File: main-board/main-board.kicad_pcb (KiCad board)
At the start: 2 copper layers, 74 parts, among them J1 NVIDIA_Jetson_NX_Dev_40pin_Co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, J10 FSESC_6.6_COMM, J11 FSESC_6.6_COMM, J12 FSESC_6.6_COMM, J13 FSESC_6.6_COMM, J14 FSESC_6.6_COMM, J2 NVIDIA_Jetson_NX_Dev_Button_C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, J3 Conn_01x02, J4 Conn_01x02, J5 Conn_01x02, J6 Conn_01x02, J7 QWIIC_Generic_Conn, J8 Conn_01x03, J9 FSESC_6.6_COMM, M1 Fan_3pin, M2 Fan_3pin, M3 Fan_3pin, Q1 Q_NMOS_GSD, Q2 Q_NMOS_GSD, Q3 Q_NMOS_GSD, Q4 Q_NMOS_GSD, Q5 Q_NMOS_GSD, Q6 Q_NMOS_GSD, Q7 Q_NMOS_GSD, Q8 Q_NMOS_GSD, U1 RFM95W_Adafruit_Breakout, U10 Analog Temp Sensor, U11 Adafruit_GPS_V3, U12 SN74AHCT125D, U2 TDK_I3A4W008A033V, U3 TDK_I3A4W008A033V, U4 PYBE30-Q24-S24, U5 Teensy_4.1, U6 Analog Temp Sensor, U7 Analog Temp Sensor, U8 Analog Temp Sensor, U9 Analog Temp Sensor

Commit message: ahhh i messed some stuff up
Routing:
- net /NX_SDA: track 55.0 -> 0.00 mm
- net /NX_SCL: track 52.3 -> 0.00 mm
- net GND: track 32.5 -> 0.09 mm
- net +5V: track 19.4 -> 0.00 mm
- net +BATT: track 16.6 -> 0.00 mm
- net +12V: track 14.7 -> 0.00 mm
- net /ADC_BATT: track 10.9 -> 0.00 mm
- net /ADC_5V: track 11.1 -> 0.76 mm
- net /ADC_12V: track 10.9 -> 0.74 mm
- net /ADC_24V: track 10.9 -> 0.74 mm
- net Net-(J8-Pad3): track 9.97 -> 0.00 mm
- net +24V: track 9.14 -> 0.00 mm
- net Net-(D12-Pad2): track 8.64 -> 0.00 mm
- net Net-(D11-Pad2): track 8.64 -> 0.00 mm
- net Net-(R5-Pad2): track 8.10 -> 0.00 mm
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
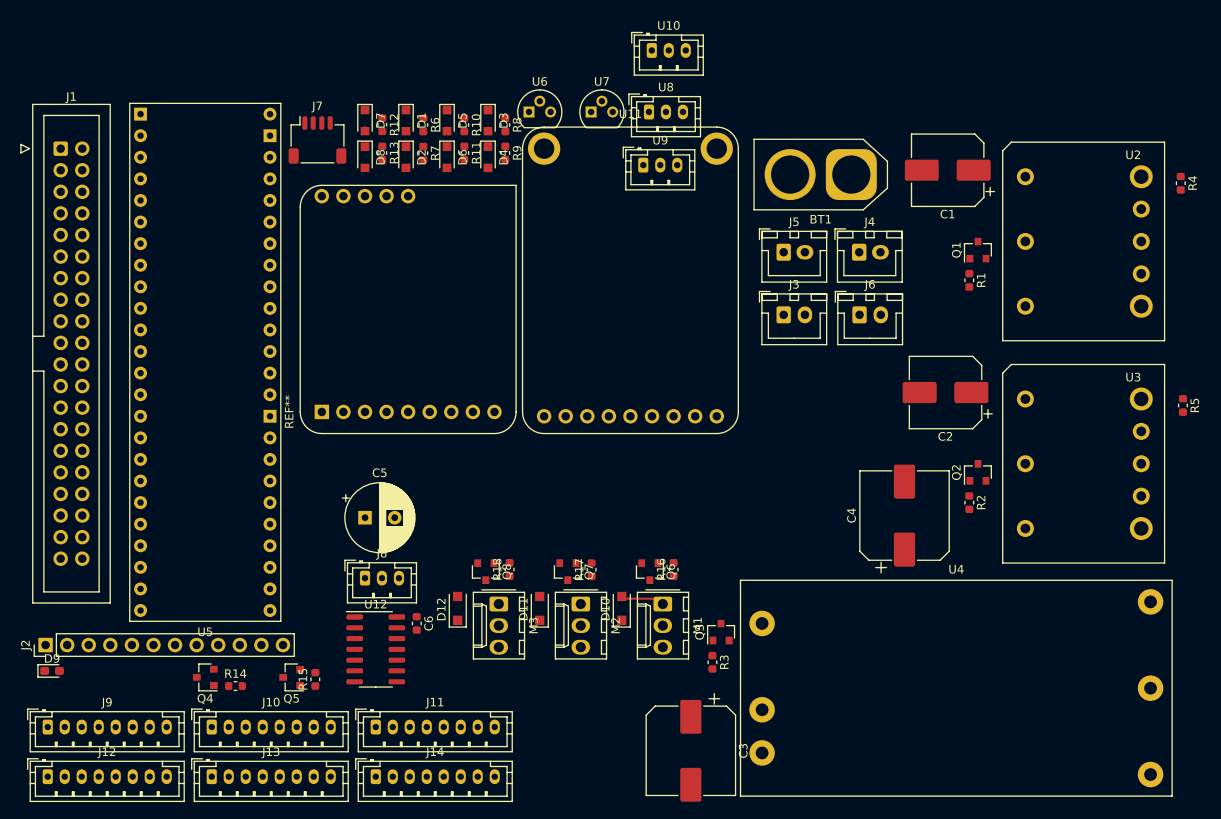
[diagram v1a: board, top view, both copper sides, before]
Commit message: Removed 24V connector, Changed net switch power bus, changed motor driver connector
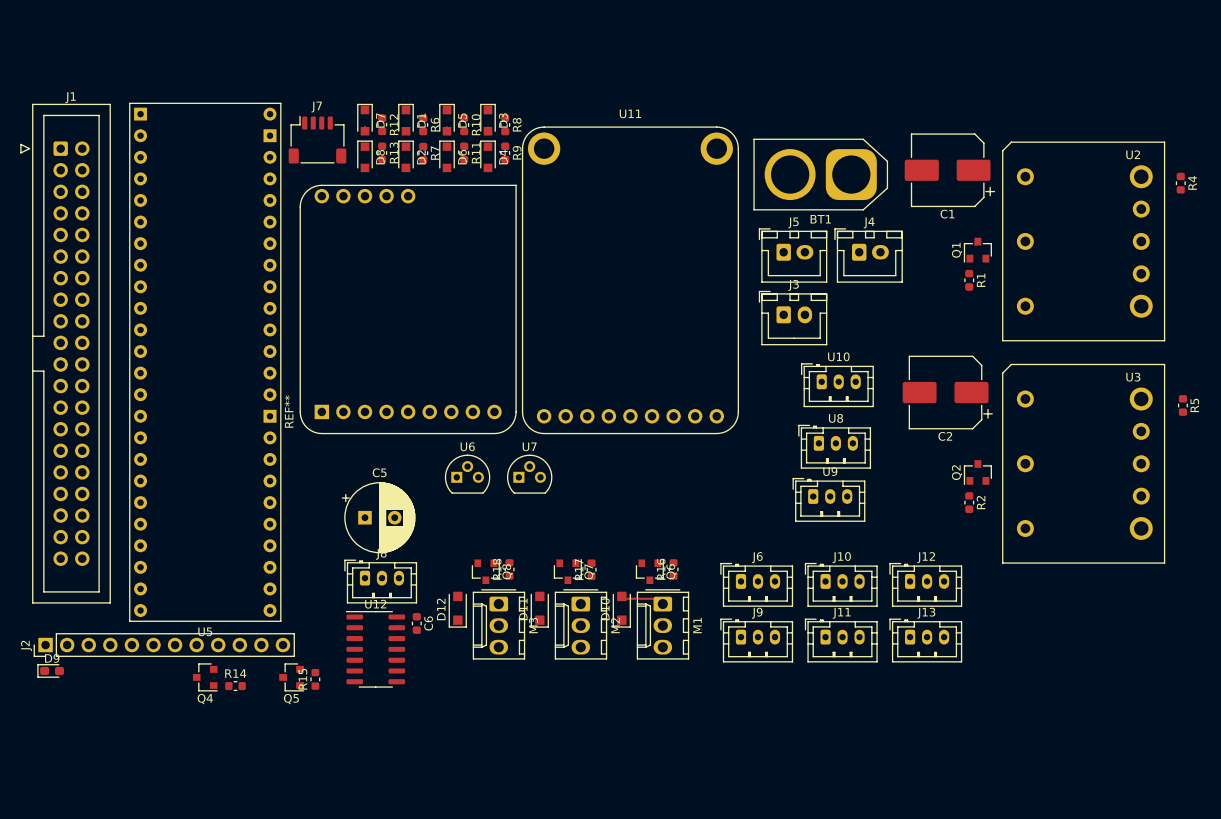
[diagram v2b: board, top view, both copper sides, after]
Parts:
- removed C3, C4: 100u, Capacitor_SMD:CP_Elec_10x10
- removed J14: FSESC_6.6_COMM, Connector_JST:JST_PH_B8B-PH-K_1x08_P2.00mm_Vertical
- removed Q3: Q_NMOS_GSD, Package_TO_SOT_SMD:SOT-23
- removed R3: 100k, Resistor_SMD:R_0603_1608Metric
- removed U4: PYBE30-Q24-S24, ASTRA_Footprints:PYBE30
- J10, J11, J12, J13, J9: value FSESC_6.6_COMM -> FSESC_6.6_COMM_Minimal; footprint Connector_JST:JST_PH_B8B-PH-K_1x08_P2.00mm_Vertical -> Connector_JST:JST_PH_B3B-PH-K_1x03_P2.00mm_Vertical
- J6: value Conn_01x02 -> FSESC_6.6_COMM_Minimal; footprint Connector_JST:JST_XH_B2B-XH-A_1x02_P2.50mm_Vertical -> Connector_JST:JST_PH_B3B-PH-K_1x03_P2.00mm_Vertical
- moved J12 104.1 mm to (127.4, 102.5)
- moved J13 83.8 mm to (127.4, 109.0)
- moved J9 82.3 mm to (107.5, 109.0)
- moved J10 74.2 mm to (117.5, 102.5)
- moved J11 54.0 mm to (117.5, 109.0)
- moved U6 43.8 mm to (74.0, 90.2)
- moved U7 43.8 mm to (81.4, 90.2)
- moved U10 43.8 mm to (117.0, 79.0)
- moved U8 43.8 mm to (116.7, 86.2)
- moved U9 43.8 mm to (116.0, 92.5)
- moved J6 34.3 mm to (107.5, 102.5)
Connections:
- J10 pad 1: Net-(J10-Pad1) -> GND
- J10 pad 2: Net-(J10-Pad2) -> /M3_RX
- J10 pad 3: GND -> /M3_TX
- J11 pad 1: Net-(J11-Pad1) -> GND
- J11 pad 2: Net-(J11-Pad2) -> /M4_RX
- J11 pad 3: GND -> /M4_TX
- J12 pad 1: Net-(J12-Pad1) -> GND
- J12 pad 2: Net-(J12-Pad2) -> /M5_RX
- J12 pad 3: GND -> /M5_TX
- J13 pad 1: Net-(J13-Pad1) -> GND
- J13 pad 2: Net-(J13-Pad2) -> /M6_RX
- J13 pad 3: GND -> /M6_TX
- J4 pad 1: +12V -> +5V
- J6 pad 1: +24V -> GND
- J6 pad 2: GND -> /M1_RX
- J9 pad 1: Net-(J9-Pad1) -> GND
- J9 pad 2: Net-(J9-Pad2) -> /M2_RX
- J9 pad 3: GND -> /M2_TX
- U5 pad 24: /24V_Disable -> Net-(U5-Pad24)
- U5 pad 44: /ADC_24V -> Net-(U5-Pad44)

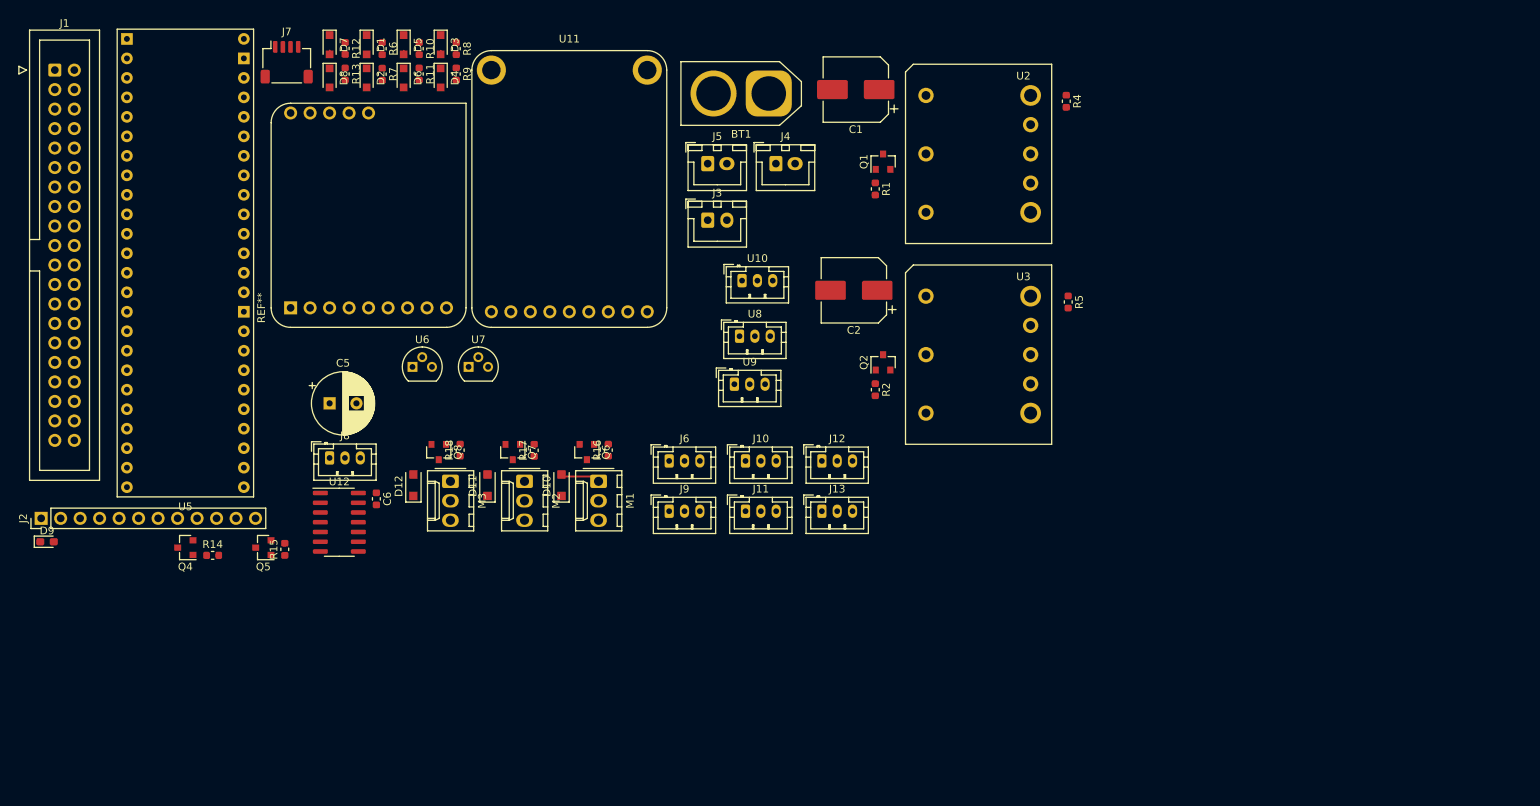
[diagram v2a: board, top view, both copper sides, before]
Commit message: Worked on PCB layout
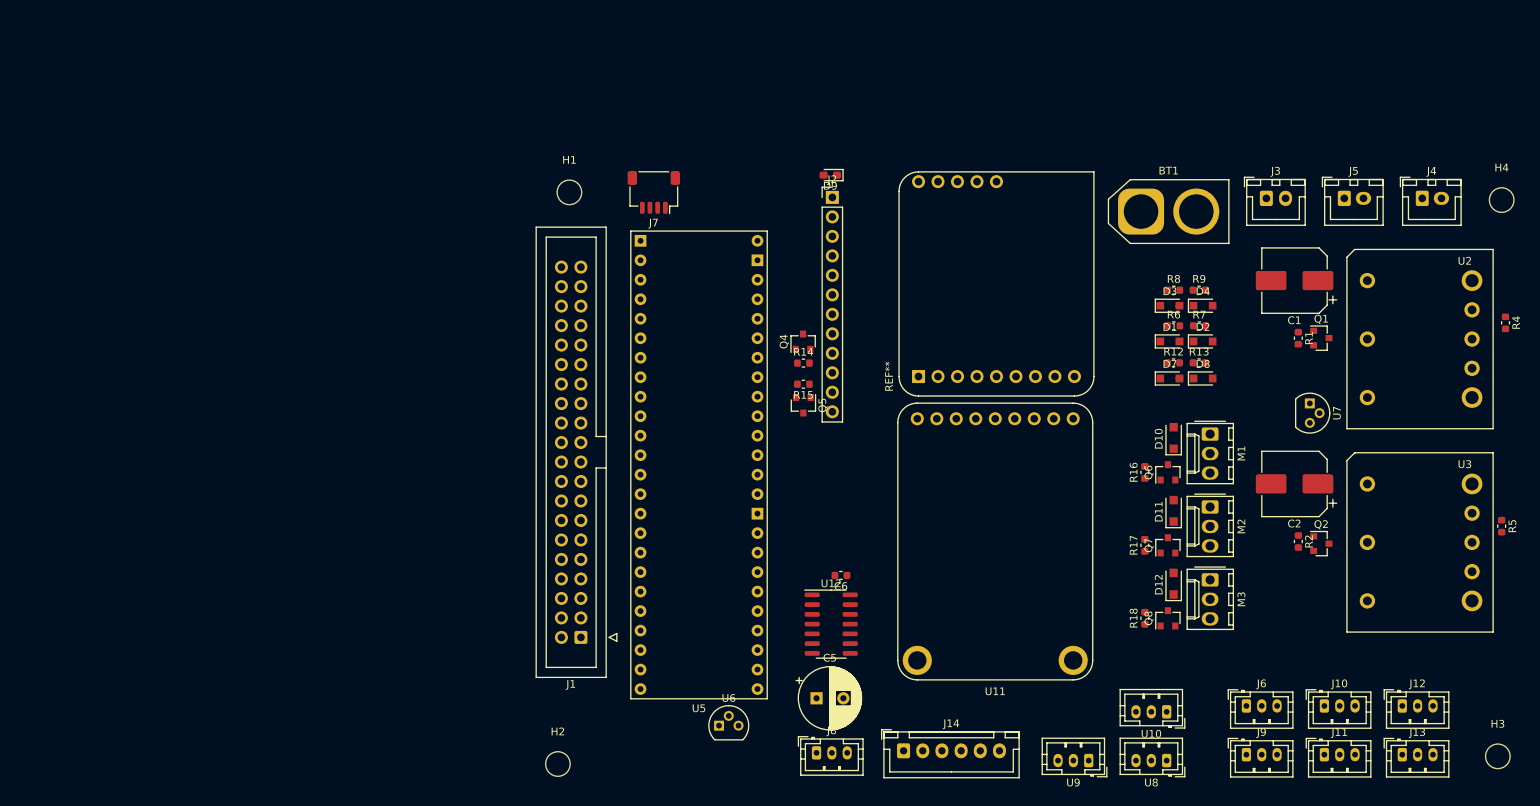
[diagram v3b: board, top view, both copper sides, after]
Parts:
- removed D5, D6: D_Schottky_Small, Diode_SMD:D_SOD-323_HandSoldering
- removed R10: 80.6k, Resistor_SMD:R_0603_1608Metric
- removed R11: 10k, Resistor_SMD:R_0603_1608Metric
- added H1: MountingHole, MountingHole:MountingHole_3.2mm_M3, F.Cu at (94.5, 67.5)
- added H2: MountingHole, MountingHole:MountingHole_3.2mm_M3, F.Cu at (93.0, 142.0)
- added H3: MountingHole, MountingHole:MountingHole_3.2mm_M3, F.Cu at (215.5, 141.0)
- added H4: MountingHole, MountingHole:MountingHole_3.2mm_M3, F.Cu at (216.0, 68.5)
- added J14: ArducamPTZ, Connector_JST:JST_XH_B6B-XH-A_1x06_P2.50mm_Vertical, F.Cu at (138.1, 140.3)
- moved D8 120.4 mm to (177.1, 91.8), turned to 0 degrees
- moved D7 117.8 mm to (172.8, 91.8), turned to 0 degrees
- moved R13 117.5 mm to (176.6, 89.7), turned to 0 degrees
- moved R12 115.5 mm to (173.2, 89.7), turned to 0 degrees
- moved D2 114.3 mm to (177.1, 86.9), turned to 0 degrees
- moved D9 112.7 mm to (128.5, 65.2), turned to 180 degrees
- moved D1 111.6 mm to (172.8, 86.9), turned to 0 degrees
- moved R7 111.4 mm to (176.6, 84.9), turned to 0 degrees
- moved J2 111.3 mm to (128.8, 68.2), turned to 0 degrees
- moved U7 109.7 mm to (191.0, 95.0), turned to 270 degrees
- moved R6 109.3 mm to (173.3, 84.9), turned to 0 degrees
- moved D4 103.7 mm to (177.1, 82.3), turned to 0 degrees
- moved D3 100.9 mm to (172.8, 82.3), turned to 0 degrees
- moved J1 100.8 mm to (96.0, 125.5), turned to 180 degrees
- moved R9 100.8 mm to (176.6, 80.2), turned to 0 degrees
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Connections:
- J1 pad 1: Net-(J1-Pad1) -> (no net)
- J1 pad 10: Net-(J1-Pad10) -> (no net)
- J1 pad 11: Net-(J1-Pad11) -> (no net)
- J1 pad 12: Net-(J1-Pad12) -> (no net)
- J1 pad 13: Net-(J1-Pad13) -> (no net)
- J1 pad 15: Net-(J1-Pad15) -> (no net)
- J1 pad 16: Net-(J1-Pad16) -> (no net)
- J1 pad 17: Net-(J1-Pad17) -> (no net)
- J1 pad 18: Net-(J1-Pad18) -> (no net)
- J1 pad 19: Net-(J1-Pad19) -> (no net)
- J1 pad 2: Net-(J1-Pad2) -> (no net)
- J1 pad 21: Net-(J1-Pad21) -> (no net)
- J1 pad 22: Net-(J1-Pad22) -> (no net)
- J1 pad 23: Net-(J1-Pad23) -> (no net)
- J1 pad 24: Net-(J1-Pad24) -> (no net)
- J1 pad 26: Net-(J1-Pad26) -> (no net)
- J1 pad 27: Net-(J1-Pad27) -> (no net)
- J1 pad 28: Net-(J1-Pad28) -> (no net)
- J1 pad 29: Net-(J1-Pad29) -> (no net)
- J1 pad 31: Net-(J1-Pad31) -> (no net)
- J1 pad 32: Net-(J1-Pad32) -> (no net)
- J1 pad 33: Net-(J1-Pad33) -> (no net)
- J1 pad 35: Net-(J1-Pad35) -> (no net)
- J1 pad 36: Net-(J1-Pad36) -> (no net)
- J1 pad 37: Net-(J1-Pad37) -> (no net)
- J1 pad 38: Net-(J1-Pad38) -> (no net)
- J1 pad 4: Net-(J1-Pad4) -> (no net)
- J1 pad 40: Net-(J1-Pad40) -> (no net)
- J1 pad 7: Net-(J1-Pad7) -> (no net)
- J1 pad 8: Net-(J1-Pad8) -> (no net)
- J2 pad 10: Net-(J2-Pad10) -> (no net)
- J2 pad 3: Net-(J2-Pad3) -> (no net)
- J2 pad 4: Net-(J2-Pad4) -> (no net)
- J2 pad 5: Net-(J2-Pad5) -> (no net)
- J2 pad 6: Net-(J2-Pad6) -> (no net)
- M1 pad 3: Net-(M1-Pad3) -> (no net)
- M2 pad 3: Net-(M2-Pad3) -> (no net)
- M3 pad 3: Net-(M3-Pad3) -> (no net)
- U1 pad 11: Net-(U1-Pad11) -> (no net)
- U1 pad 12: Net-(U1-Pad12) -> (no net)
- U1 pad 13: Net-(U1-Pad13) -> (no net)
- U1 pad 14: Net-(U1-Pad14) -> (no net)
- U1 pad 15: Net-(U1-Pad15) -> (no net)
- U1 pad 3: Net-(U1-Pad3) -> (no net)
- U11 pad 1: Net-(U11-Pad1) -> (no net)
- U11 pad 2: Net-(U11-Pad2) -> (no net)
- U11 pad 3: Net-(U11-Pad3) -> (no net)
- U11 pad 4: Net-(U11-Pad4) -> (no net)
- U11 pad 9: Net-(U11-Pad9) -> (no net)
- U2 pad 5: Net-(U2-Pad5) -> (no net)
- U3 pad 5: Net-(U3-Pad5) -> (no net)
- U5 pad 11: Net-(U5-Pad11) -> (no net)
- U5 pad 15: Net-(U5-Pad15) -> (no net)
- U5 pad 24: Net-(U5-Pad24) -> (no net)
- U5 pad 38: Net-(U5-Pad38) -> (no net)
- U5 pad 39: Net-(U5-Pad39) -> (no net)
- U5 pad 44: Net-(U5-Pad44) -> (no net)
- U5 pad 45: Net-(U5-Pad45) -> (no net)
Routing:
- net Net-(D10-Pad2): track 5.09 -> 0.00 mm
- net /ADC_24V: track 0.74 -> 0.00 mm

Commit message: Started routing
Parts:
- moved J7 65.3 mm to (99.0, 132.5), turned to 270 degrees
- moved D4 59.1 mm to (123.1, 106.3)
- moved R8 59.1 mm to (119.3, 104.2)
- moved R9 59.1 mm to (122.6, 104.2)
- moved D3 59.1 mm to (118.8, 106.3)
- moved D8 57.2 mm to (123.1, 110.8)
- moved R12 57.2 mm to (119.2, 108.7)
- moved R13 57.2 mm to (122.6, 108.7)
- moved D7 57.2 mm to (118.8, 110.8)
- moved D2 56.0 mm to (123.1, 101.9)
- moved R6 56.0 mm to (119.3, 99.9)
- moved D1 56.0 mm to (118.8, 101.9)
- moved R7 56.0 mm to (122.6, 99.9)
- moved Q5 49.0 mm to (105.5, 140.2)
- moved R14 49.0 mm to (105.5, 134.8)
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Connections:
- U5 pad 16: /GPS_TX -> GND
- U5 pad 17: /GPS_RX -> /M3_TX
- U5 pad 18: /ADC3 -> /SCK
- U5 pad 19: /ADC4 -> /M3_RX
- U5 pad 20: /M5_RX -> (no net)
- U5 pad 21: /M5_TX -> (no net)
- U5 pad 22: /12V_Disable -> /ADC1
- U5 pad 23: /5V_Disable -> /ADC2
- U5 pad 24: (no net) -> /M4_TX
- U5 pad 25: /Fan1_Control -> /M4_RX
- U5 pad 26: /M6_RX -> (no net)
- U5 pad 27: /M6_TX -> (no net)
- U5 pad 28: /Fan2_Control -> +3V3
- U5 pad 29: /Fan3_Control -> GND
- U5 pad 30: /ADC_5V -> +5V
- U5 pad 31: /ADC_12V -> /GPS_TX
- U5 pad 32: /ADC_BATT -> /GPS_RX
- U5 pad 33: /ADC5 -> /ADC3
- U5 pad 34: GND -> /ADC4
- U5 pad 35: /SCK -> /M5_RX
- U5 pad 36: /M3_TX -> /M5_TX
- U5 pad 37: /M3_RX -> /12V_Disable
- U5 pad 38: (no net) -> /5V_Disable
- U5 pad 40: /ADC1 -> /Fan1_Control
- U5 pad 41: /ADC2 -> /M6_RX
- U5 pad 42: /M4_TX -> /M6_TX
- U5 pad 43: /M4_RX -> /Fan2_Control
- U5 pad 44: (no net) -> /Fan3_Control
- U5 pad 45: (no net) -> /ADC_5V
- U5 pad 46: +3V3 -> /ADC_12V
- U5 pad 47: GND -> /ADC_BATT
- U5 pad 48: +5V -> /ADC5
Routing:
- net +5V: track 0.00 -> 352.9 mm
- net +12V: track 0.00 -> 110.5 mm, vias 0 -> 2
- net Net-(Q1-Pad3): track 0.00 -> 11.0 mm, vias 0 -> 1
- net Net-(D12-Pad2): track 0.00 -> 10.7 mm
- net Net-(D11-Pad2): track 0.00 -> 10.7 mm
- net Net-(D10-Pad2): track 0.00 -> 10.7 mm
- net Net-(R5-Pad2): track 0.00 -> 5.41 mm
- net Net-(R4-Pad2): track 0.00 -> 5.41 mm
- added copper zone on F.Cu, net +BATT
- added copper zone on F.Cu, net GND
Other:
- board outline added: 117 x 83 mm
- net class Default: clearance 0.2 -> 0.1524; trace_width 0.25 -> 0.1524; via_dia 0.8 -> 0.508; via_drill 0.4 -> 0.254
- rule pad_to_mask_clearance: 0 -> 0.0508
- rule trace_clearance: 0.2 -> 0.1524
- rule trace_min: 0.2 -> 0.1524
- rule via_min_drill: 0.3 -> 0.254
- rule via_min_size: 0.4 -> 0.508

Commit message: Shooouuulld be fully routed
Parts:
- added J15: Angle Sensor, Connector_JST:JST_PH_B6B-PH-K_1x06_P2.00mm_Vertical, F.Cu at (172.0, 125.0)
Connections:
- U5 pad 10: /M2_TX -> /M4_TX
- U5 pad 11: (no net) -> /Angle_CS
- U5 pad 2: /M1_RX -> /M6_RX
- U5 pad 24: /M4_TX -> /M5_TX
- U5 pad 25: /M4_RX -> /M5_RX
- U5 pad 3: /M1_TX -> /M6_TX
- U5 pad 33: /ADC3 -> /ADC5
- U5 pad 35: /M5_RX -> /M2_RX
- U5 pad 36: /M5_TX -> /M2_TX
- U5 pad 41: /M6_RX -> /M1_RX
- U5 pad 42: /M6_TX -> /M1_TX
- U5 pad 45: /ADC_5V -> /ADC3
- U5 pad 46: /ADC_12V -> /ADC_5V
- U5 pad 47: /ADC_BATT -> /ADC_12V
- U5 pad 48: /ADC5 -> /ADC_BATT
- U5 pad 9: /M2_RX -> /M4_RX
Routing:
- net +3V3: track 0.00 -> 224.6 mm, vias 0 -> 3
- net /M6_RX: track 0.00 -> 141.2 mm
- net /M6_TX: track 0.00 -> 138.6 mm
- net /M5_RX: track 0.00 -> 117.1 mm, vias 0 -> 1
- net /M5_TX: track 0.00 -> 115.7 mm
- net /M4_RX: track 0.00 -> 112.6 mm
- net /M4_TX: track 0.00 -> 109.3 mm
- net /12V_Disable: track 0.00 -> 102.2 mm, vias 0 -> 8
- net /MISO: track 0.00 -> 96.9 mm, vias 0 -> 1
- net /MOSI: track 0.00 -> 95.7 mm, vias 0 -> 1
- net /Angle_CS: track 0.00 -> 94.0 mm, vias 0 -> 3
- net /M3_RX: track 0.00 -> 91.7 mm
- net /M3_TX: track 0.00 -> 88.3 mm, vias 0 -> 1
- net /5V_Disable: track 0.00 -> 82.9 mm, vias 0 -> 8
- net /SCK: track 0.00 -> 82.2 mm
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- added copper zone on B.Cu, net GND

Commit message: DONE! (hopefully)
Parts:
- added G***: LOGO, ASTRA_Footprints:ATRALogo, B.Cu at (145.6, 111.6)
- added G***: LOGO, ASTRA_Footprints:SHCLogo, B.Cu at (152.2, 74.6)
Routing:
- net GND: vias 156 -> 178
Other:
- board text added: "1 2 3"
- board text added: "12 V Jetson"
- board text added: "12 V PTZ"
- board text added: "5 V Net Switch"
- board text added: "Battery Input"
- board text added: "Ext Therm"
- board text added: "Motor AUX1"
- board text added: "Motor AUX2"
- board text added: "Motor BL"
- board text added: "Motor BR"
- board text added: "Motor FL"
- board text added: "Motor FR"
- board text added: "Neopixel"
- board text added: "PTZ Control"
- board text added: "Susp. Angle Sensor"
- board text added: "UAH SHC ASTRA Rover PCB V1 Sep 2021"
